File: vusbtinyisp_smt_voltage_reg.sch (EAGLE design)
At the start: 9 parts, among them IC1 MCP170333MB, U2 TINY45-20-DIP

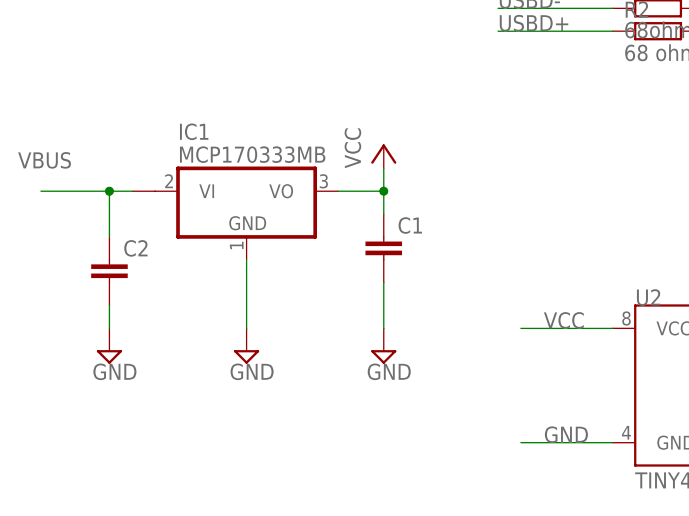
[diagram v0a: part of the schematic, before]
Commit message: changing 1k to 1.5k resistors in 5V designs
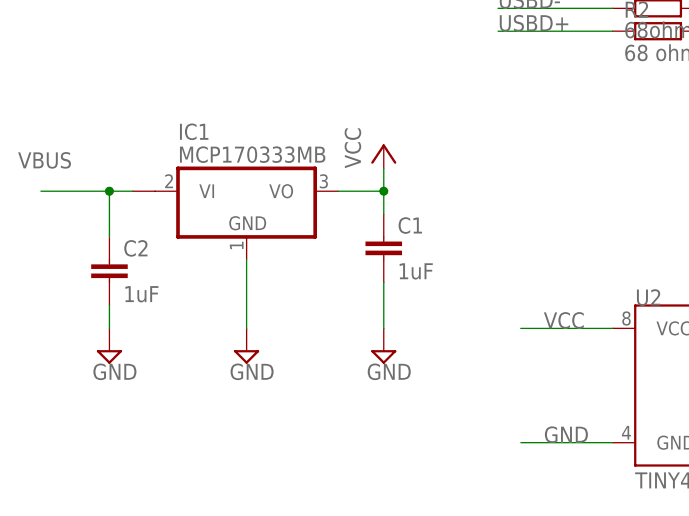
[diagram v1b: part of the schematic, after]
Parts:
- C1, C2: value (none) -> 1uF
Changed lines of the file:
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@@
 </classes>
 <parts>
-<part name="C1" library="SparkFun-Passives" deviceset="CAP" device="1206"/>
+<part name="C1" library="SparkFun-Passives" deviceset="CAP" device="1206" value="1uF"/>
 <part name="SUPPLY1" library="supply2" deviceset="GND" device=""/>
 <part name="USB" library="pinhead" deviceset="PINHD-1X4" device=""/>
@@
 <part name="R3" library="resistor" deviceset="R-EU_" device="R1206" value="1k Ohm"/>
 <part name="U$1" library="elliot" deviceset="SMT_ISP" device=""/>
-<part name="C2" library="SparkFun-Passives" deviceset="CAP" device="1206"/>
+<part name="C2" library="SparkFun-Passives" deviceset="CAP" device="1206" value="1uF"/>
 <part name="P+3" library="supply1" deviceset="VCC" device=""/>
 <part name="SUPPLY4" library="supply2" deviceset="GND" device=""/>
